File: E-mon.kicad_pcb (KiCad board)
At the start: 2 copper layers, 85.1 x 43.8 mm, 40 parts, among them J1 USB_B_Micro, J2 RJ18, Q1 MMBF170, Q2 MMBF170, Q3 MMBT5550L, Q4 MMBT5550L, SW1 SW_Push, U1 CP2104, U2 MCP1640BCH, U3 MCP73831-2-OT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

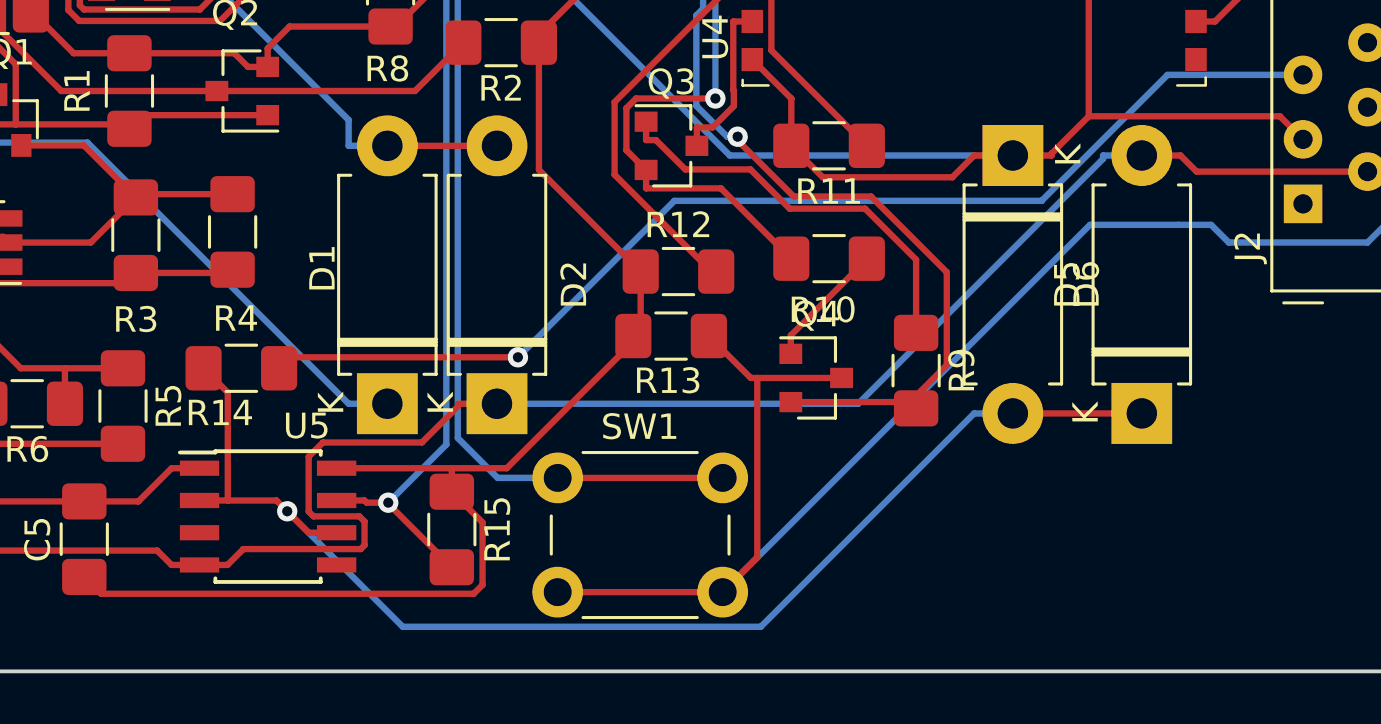
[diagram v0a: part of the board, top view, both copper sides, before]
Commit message: pcb: fix various routing issues
Fix some poorly routed tracks.

Signed-off-by: Michel Megens <dev@bietje.net>
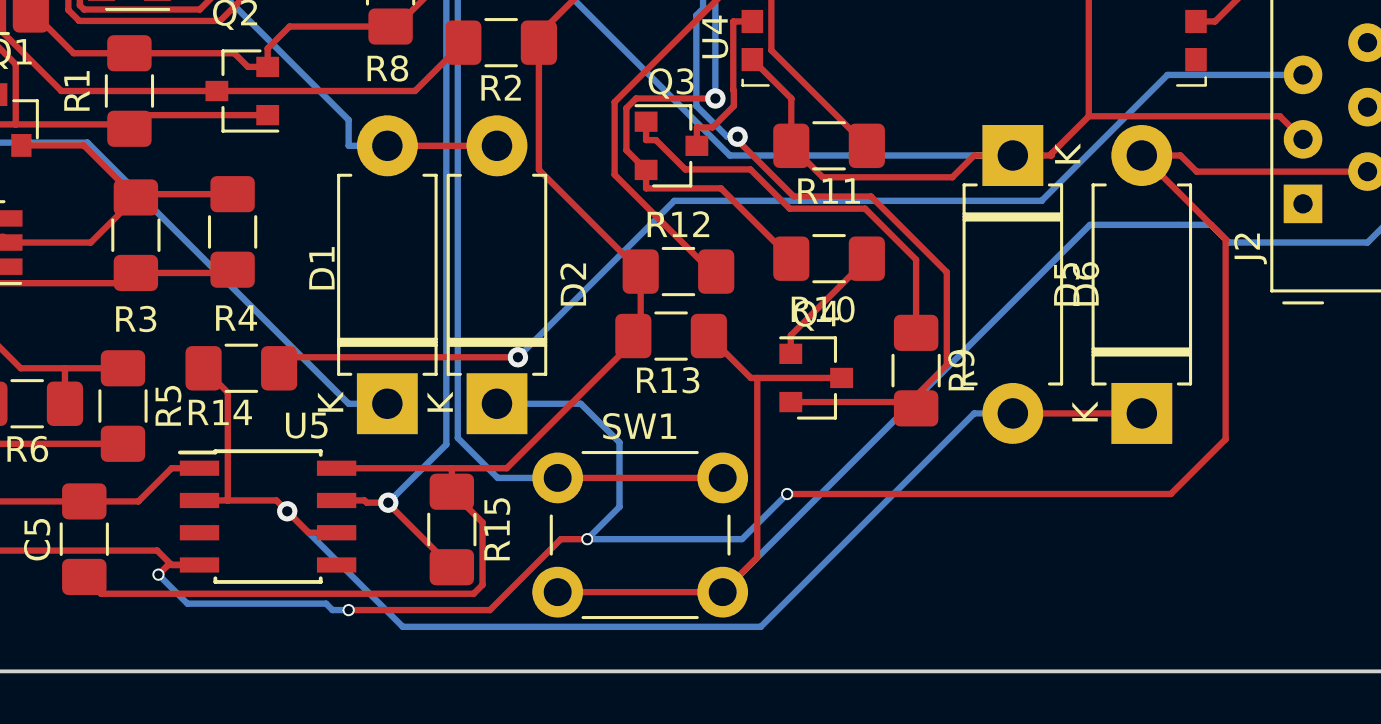
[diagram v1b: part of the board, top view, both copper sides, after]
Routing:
- net VBUS: track 159.5 -> 179.5 mm, vias 0 -> 4
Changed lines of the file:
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@@
     (thickness 1.6)
     (drawings 5)
-    (tracks 454)
+    (tracks 459)
     (zones 0)
     (modules 40)
@@
   (segment (start 84.803 122.174) (end 83.7027 122.174) (width 0.25) (layer F.Cu) (net 8))
   (segment (start 85.3532 122.174) (end 84.803 122.174) (width 0.25) (layer F.Cu) (net 8))
-  (segment (start 85.3532 122.174) (end 85.9033 122.174) (width 0.25) (layer F.Cu) (net 8))
   (segment (start 76.2477 105.648) (end 75.885 105.648) (width 0.25) (layer F.Cu) (net 8))
   (segment (start 75.1 108.524) (end 75.7687 108.524) (width 0.25) (layer F.Cu) (net 8))
   (segment (start 76.2477 105.648) (end 76.6103 105.648) (width 0.25) (layer F.Cu) (net 8))
-  (segment (start 96.52 115.824) (end 110.7475 115.824) (width 0.25) (layer B.Cu) (net 8))
-  (segment (start 110.7475 115.824) (end 120.3947 106.1768) (width 0.25) (layer B.Cu) (net 8))
-  (segment (start 120.3947 106.1768) (end 120.3947 106.045) (width 0.25) (layer B.Cu) (net 8))
-  (segment (start 121.92 106.045) (end 120.3947 106.045) (width 0.25) (layer B.Cu) (net 8))
   (segment (start 76.6103 105.648) (end 76.6103 104.8464) (width 0.25) (layer F.Cu) (net 8))
   (segment (start 76.6103 104.8464) (end 76.6367 104.82) (width 0.25) (layer F.Cu) (net 8))
@@
   (segment (start 123.4453 106.045) (end 124.0803 106.68) (width 0.25) (layer F.Cu) (net 8))
   (segment (start 124.0803 106.68) (end 130.81 106.68) (width 0.25) (layer F.Cu) (net 8))
-  (segment (start 96.52 115.824) (end 94.9947 115.824) (width 0.25) (layer F.Cu) (net 8))
-  (segment (start 94.9947 115.824) (end 94.9947 115.9195) (width 0.25) (layer F.Cu) (net 8))
-  (segment (start 94.9947 115.9195) (end 93.5649 117.3493) (width 0.25) (layer F.Cu) (net 8))
-  (segment (start 93.5649 117.3493) (end 89.6634 117.3493) (width 0.25) (layer F.Cu) (net 8))
-  (segment (start 89.6634 117.3493) (end 89.1026 117.9101) (width 0.25) (layer F.Cu) (net 8))
-  (segment (start 89.1026 117.9101) (end 89.1026 120.0687) (width 0.25) (layer F.Cu) (net 8))
-  (segment (start 89.1026 120.0687) (end 89.2933 120.2594) (width 0.25) (layer F.Cu) (net 8))
-  (segment (start 89.2933 120.2594) (end 91.1016 120.2594) (width 0.25) (layer F.Cu) (net 8))
-  (segment (start 91.1016 120.2594) (end 91.3034 120.4612) (width 0.25) (layer F.Cu) (net 8))
-  (segment (start 91.3034 120.4612) (end 91.3034 121.3959) (width 0.25) (layer F.Cu) (net 8))
-  (segment (start 91.3034 121.3959) (end 91.1506 121.5487) (width 0.25) (layer F.Cu) (net 8))
-  (segment (start 91.1506 121.5487) (end 86.5286 121.5487) (width 0.25) (layer F.Cu) (net 8))
-  (segment (start 86.5286 121.5487) (end 85.9033 122.174) (width 0.25) (layer F.Cu) (net 8))
   (segment (start 87.487 104.455) (end 82.5795 104.455) (width 0.25) (layer F.Cu) (net 8))
   (segment (start 82.5795 104.455) (end 82.042 104.9925) (width 0.25) (layer F.Cu) (net 8))
+  (segment (start 84.803 122.174) (end 83.566 122.174) (width 0.25) (layer F.Cu) (net 8))
+  (via (at 83.185 122.555) (size 0.4826) (drill 0.3302) (layers F.Cu B.Cu) (net 8))
+  (segment (start 83.566 122.174) (end 83.185 122.555) (width 0.25) (layer F.Cu) (net 8))
+  (segment (start 83.185 122.555) (end 84.328 123.698) (width 0.25) (layer B.Cu) (net 8))
+  (segment (start 84.328 123.698) (end 89.789 123.698) (width 0.25) (layer B.Cu) (net 8))
+  (via (at 90.678 123.952) (size 0.4826) (drill 0.3302) (layers F.Cu B.Cu) (net 8))
+  (segment (start 89.789 123.698) (end 90.043 123.952) (width 0.25) (layer B.Cu) (net 8))
+  (segment (start 90.043 123.952) (end 90.678 123.952) (width 0.25) (layer B.Cu) (net 8))
+  (segment (start 90.678 123.952) (end 96.241998 123.952) (width 0.25) (layer F.Cu) (net 8))
+  (segment (start 96.241998 123.952) (end 99.035998 121.158) (width 0.25) (layer F.Cu) (net 8))
+  (segment (start 123.063 119.38) (end 125.222 117.221) (width 0.25) (layer F.Cu) (net 8))
+  (segment (start 125.222 117.221) (end 125.222 109.347) (width 0.25) (layer F.Cu) (net 8))
+  (segment (start 125.222 109.347) (end 121.92 106.045) (width 0.25) (layer F.Cu) (net 8))
+  (segment (start 107.95 119.38) (end 123.063 119.38) (width 0.25) (layer F.Cu) (net 8))
+  (via (at 107.95 119.38) (size 0.4826) (drill 0.3302) (layers F.Cu B.Cu) (net 8))
+  (via (at 100.076 121.158) (size 0.4826) (drill 0.3302) (layers F.Cu B.Cu) (net 8))
+  (segment (start 99.035998 121.158) (end 100.076 121.158) (width 0.25) (layer F.Cu) (net 8))
+  (segment (start 106.172 121.158) (end 107.95 119.38) (width 0.25) (layer B.Cu) (net 8))
+  (segment (start 100.076 121.158) (end 106.172 121.158) (width 0.25) (layer B.Cu) (net 8))
+  (segment (start 101.346 119.888) (end 100.076 121.158) (width 0.25) (layer B.Cu) (net 8))
+  (segment (start 101.346 117.348) (end 101.346 119.888) (width 0.25) (layer B.Cu) (net 8))
+  (segment (start 96.52 115.824) (end 99.822 115.824) (width 0.25) (layer B.Cu) (net 8))
+  (segment (start 99.822 115.824) (end 101.346 117.348) (width 0.25) (layer B.Cu) (net 8))
   (segment (start 74.0045 114.554) (end 75.257 114.554) (width 0.25) (layer F.Cu) (net 9))
   (segment (start 75.257 114.554) (end 76.527 115.824) (width 0.25) (layer F.Cu) (net 9))

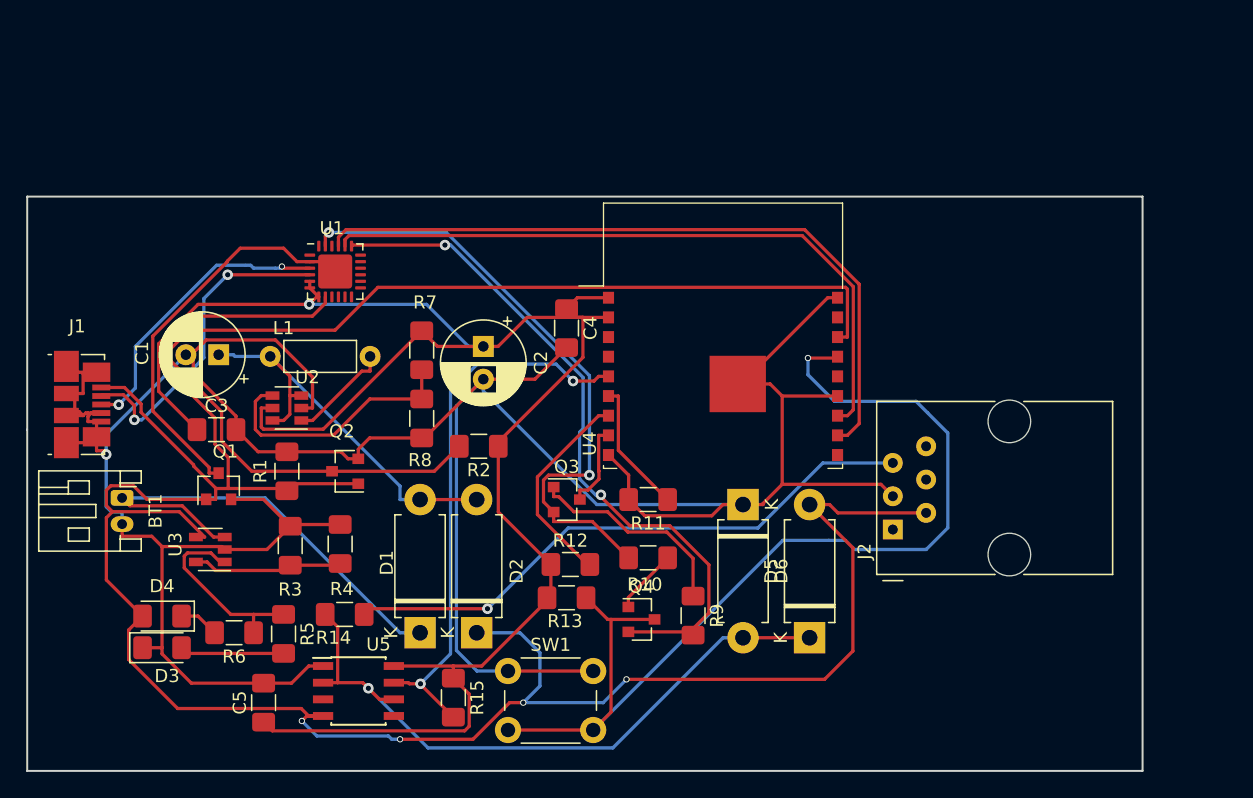
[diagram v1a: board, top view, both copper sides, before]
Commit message: pcb: add ground plane
Add the ground plane to both layers.

Signed-off-by: Michel Megens <dev@bietje.net>
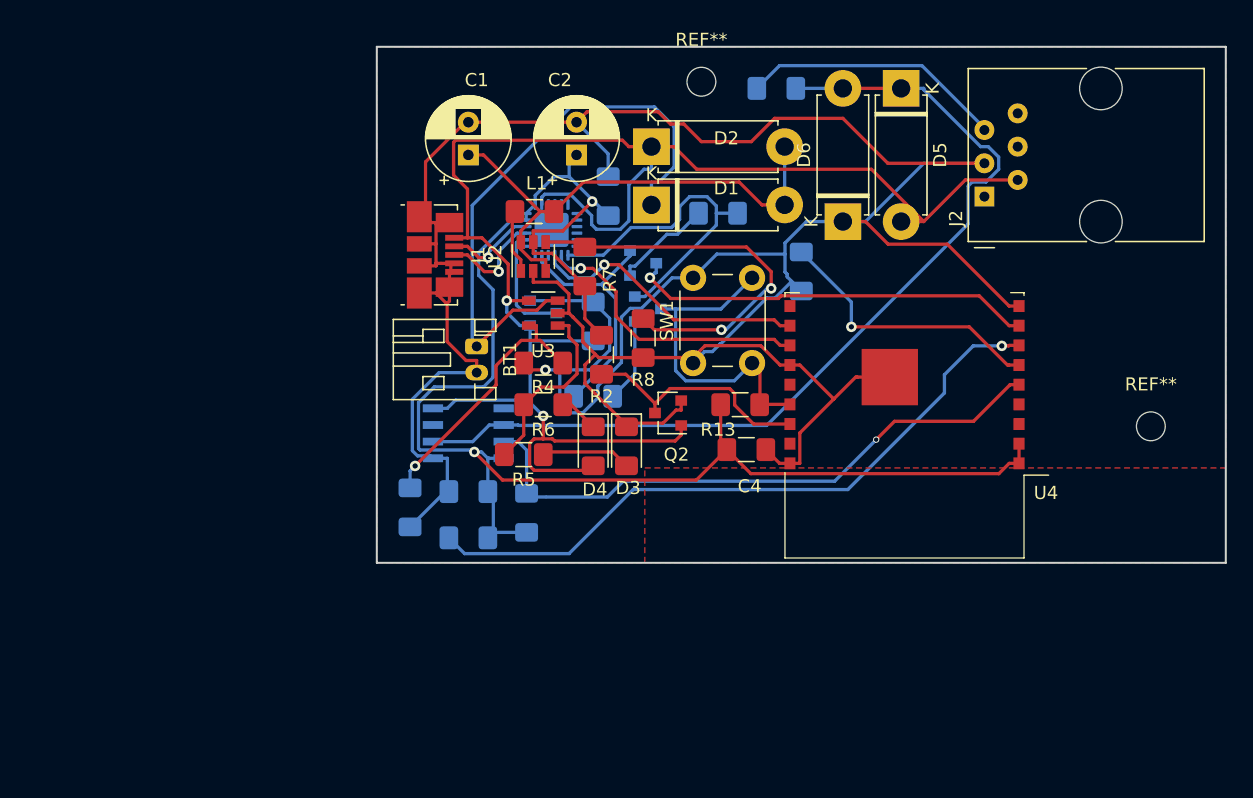
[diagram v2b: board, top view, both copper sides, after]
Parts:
- added REF**: MountingHole_2.2mm_M2, MountingHole:MountingHole_2.2mm_M2, F.Cu at (113.7, 73.8)
- added REF**: MountingHole_2.2mm_M2, MountingHole:MountingHole_2.2mm_M2, F.Cu at (148.0, 100.1)
- C3, C5, Q1, Q3, Q4, R1, R10, R11, R12, R14, R15, R3, R9, U1, U5: moved to B.Cu
- D1, D2, D5, D6: footprint Diode_THT:D_DO-15_P10.16mm_Horizontal -> Diode_THT:D_5W_P10.16mm_Horizontal
- L1: footprint Inductor_THT:L_Axial_L5.3mm_D2.2mm_P7.62mm_Horizontal_Vishay_IM-1 -> Inductor_SMD:L_1206_3216Metric_Pad1.42x1.75mm_HandSolder
- moved R14 51.9 mm to (119.4, 74.3), turned to 180 degrees
- moved D5 42.5 mm to (128.9, 74.3), turned to 270 degrees
- moved D2 39.4 mm to (109.9, 78.7), turned to 0 degrees
- moved D3 38.6 mm to (108.0, 101.6), turned to 270 degrees
- moved D1 37.1 mm to (109.9, 83.2), turned to 0 degrees
- moved D4 35.4 mm to (105.4, 101.6), turned to 270 degrees
- moved C3 34.8 mm to (106.6, 82.5), turned to 90 degrees
- moved U3 31.2 mm to (101.6, 91.4)
- moved R9 30.8 mm to (114.9, 83.8), turned to 0 degrees
- moved BT1 29.4 mm to (96.5, 94.0)
- moved R6 29.3 mm to (101.6, 98.4), turned to 0 degrees
- moved J1 29.2 mm to (93.3, 87.0)
- moved Q1 28.1 mm to (101.6, 91.4), turned to 0 degrees
- moved SW1 27.4 mm to (113.0, 95.2), turned to 90 degrees
- moved J2 26.3 mm to (135.3, 82.5)
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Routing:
- net Vadap: track 86.6 -> 18.1 mm
- net RESET: track 78.8 -> 25.1 mm, vias 1 -> 0
- net VBUS: track 179.5 -> 125.9 mm, vias 4 -> 2
- net Net-(R12-Pad2): track 15.8 -> 51.4 mm, vias 0 -> 1
- net PROG_RX0: track 55.0 -> 21.4 mm, vias 0 -> 1
- net PROG_TX0: track 51.8 -> 21.7 mm, vias 0 -> 1
- net DTR: track 47.2 -> 19.6 mm, vias 2 -> 0
- net RTS: track 53.1 -> 25.6 mm, vias 2 -> 0
- net Net-(J2-Pad5): track 45.1 -> 20.2 mm, vias 1 -> 0
- net GPIO_0: track 6.62 -> 31.2 mm, vias 0 -> 1
- net Net-(D5-Pad1): track 50.6 -> 72.1 mm, vias 1 -> 0
- net Net-(Q1-Pad3): track 30.4 -> 11.1 mm
- net +3V3: track 137.0 -> 118.2 mm, vias 1 -> 2
- net D_NEG: track 24.6 -> 7.05 mm, vias 2 -> 1
- net D_PLUS: track 22.4 -> 8.13 mm, vias 2 -> 1
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- added copper zone on B.Cu, net GND
- added copper zone on F.Cu, net GND
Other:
- board size 85.1 x 43.8 mm -> 64.8 x 39.4 mm

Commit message: 555: update Vcc connection of the NE555
Connect the NE555 to the Vbus (5V) instead of 3.3V.

Signed-off-by: Michel Megens <dev@bietje.net>
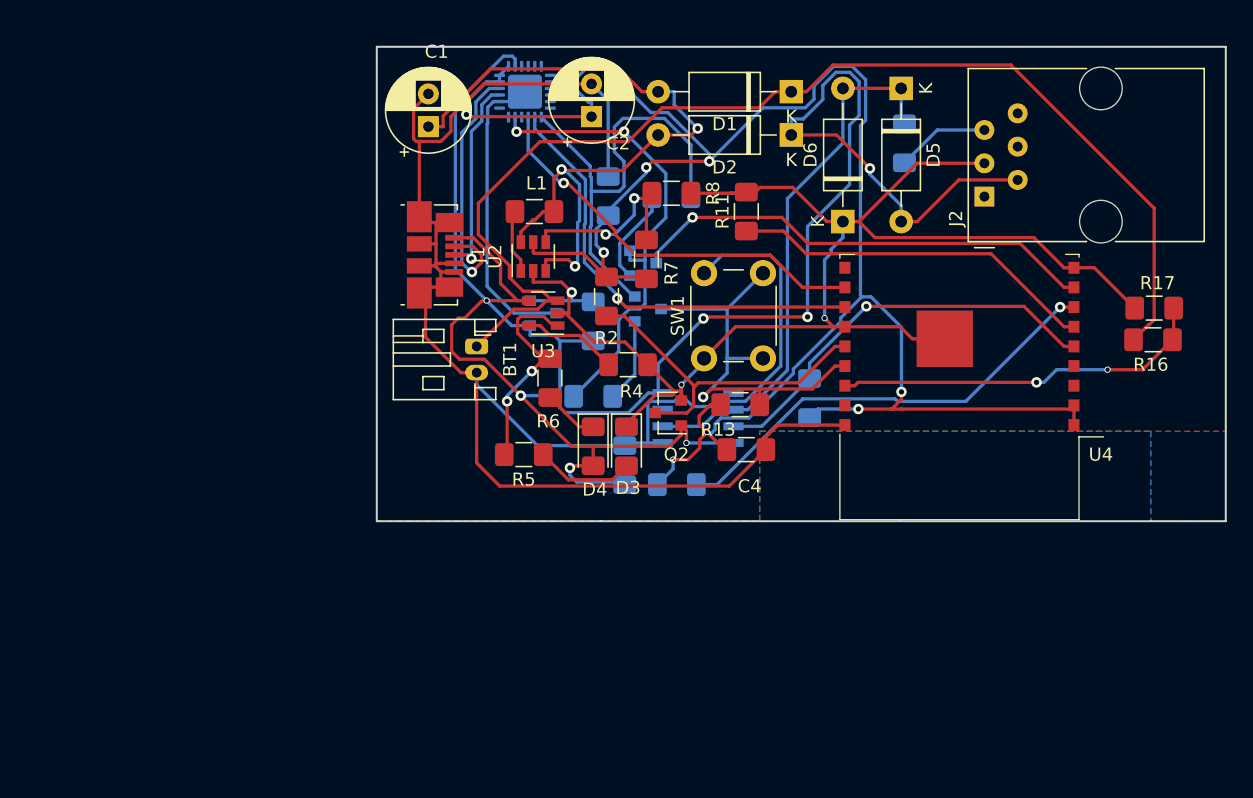
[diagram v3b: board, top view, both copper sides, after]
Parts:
- removed R3: 2.5kΩ, Resistor_SMD:R_1206_3216Metric_Pad1.42x1.75mm_HandSolder
- removed REF** (x2): MountingHole_2.2mm_M2, MountingHole:MountingHole_2.2mm_M2
- added R16: 100kΩ, Resistor_SMD:R_1206_3216Metric_Pad1.42x1.75mm_HandSolder, F.Cu at (148.1, 93.5)
- added R17: 100kΩ, Resistor_SMD:R_1206_3216Metric_Pad1.42x1.75mm_HandSolder, F.Cu at (148.2, 91.1)
- D1, D2, D5, D6: footprint Diode_THT:D_5W_P10.16mm_Horizontal -> Diode_THT:D_A-405_P10.16mm_Horizontal
- R11: moved to F.Cu
- moved R15 23.3 mm to (121.9, 97.9)
- moved U5 17.6 mm to (113.4, 99.4)
- moved R12 16.4 mm to (111.8, 104.5), turned to 0 degrees
- moved D1 13.7 mm to (120.5, 74.5), turned to 180 degrees
- moved C5 12.1 mm to (107.8, 103.0), turned to 90 degrees
- moved R8 11.3 mm to (111.4, 82.3), turned to 0 degrees
- moved U1 10.7 mm to (100.2, 74.5)
- moved D2 10.7 mm to (120.5, 77.9), turned to 180 degrees
- moved R14 10.6 mm to (129.2, 78.5), turned to 270 degrees
- moved R4 6.48 mm to (108.1, 95.4), turned to 0 degrees
- moved R11 6.20 mm to (117.1, 83.7), turned to 90 degrees
- moved U4 5.11 mm to (133.3, 94.0)
- moved R7 4.73 mm to (109.5, 87.3)
- moved R2 4.46 mm to (106.4, 90.2)
- moved R9 3.78 mm to (111.4, 82.5)
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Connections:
- C5 pad 1: +3V3 -> VBUS
- U4 pad 14: Net-(U4-Pad14) -> Vadap
- U4 pad 16: Vadap -> ADC
- U5 pad 8: +3V3 -> VBUS
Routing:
- net +BATT: track 44.7 -> 89.4 mm
- net VBUS: track 125.9 -> 166.0 mm, vias 2 -> 7
- net +3V3: track 118.2 -> 152.4 mm, vias 2 -> 8
- net Net-(D5-Pad1): track 72.1 -> 41.8 mm
- net ADC: track 0.00 -> 29.0 mm, vias 0 -> 2
- net Net-(C1-Pad1): track 38.6 -> 56.0 mm, vias 0 -> 3
- net Net-(R12-Pad2): track 51.4 -> 34.6 mm
- net Net-(R7-Pad2): track 30.8 -> 14.3 mm
- net DTR: track 19.6 -> 36.1 mm, vias 0 -> 2
- net EMON_RX: track 46.5 -> 31.7 mm
- net Net-(J2-Pad5): track 20.2 -> 7.13 mm
- net Net-(R4-Pad1): track 20.4 -> 7.33 mm, vias 1 -> 0
- net D_NEG: track 7.05 -> 20.0 mm
- net PROG_TX0: track 21.7 -> 34.1 mm
- net Net-(Q1-Pad3): track 11.1 -> 23.1 mm
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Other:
- board size 64.8 x 39.4 mm -> 64.8 x 36.2 mm
